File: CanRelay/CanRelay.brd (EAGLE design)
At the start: 93 x 65.5 mm, 21 parts

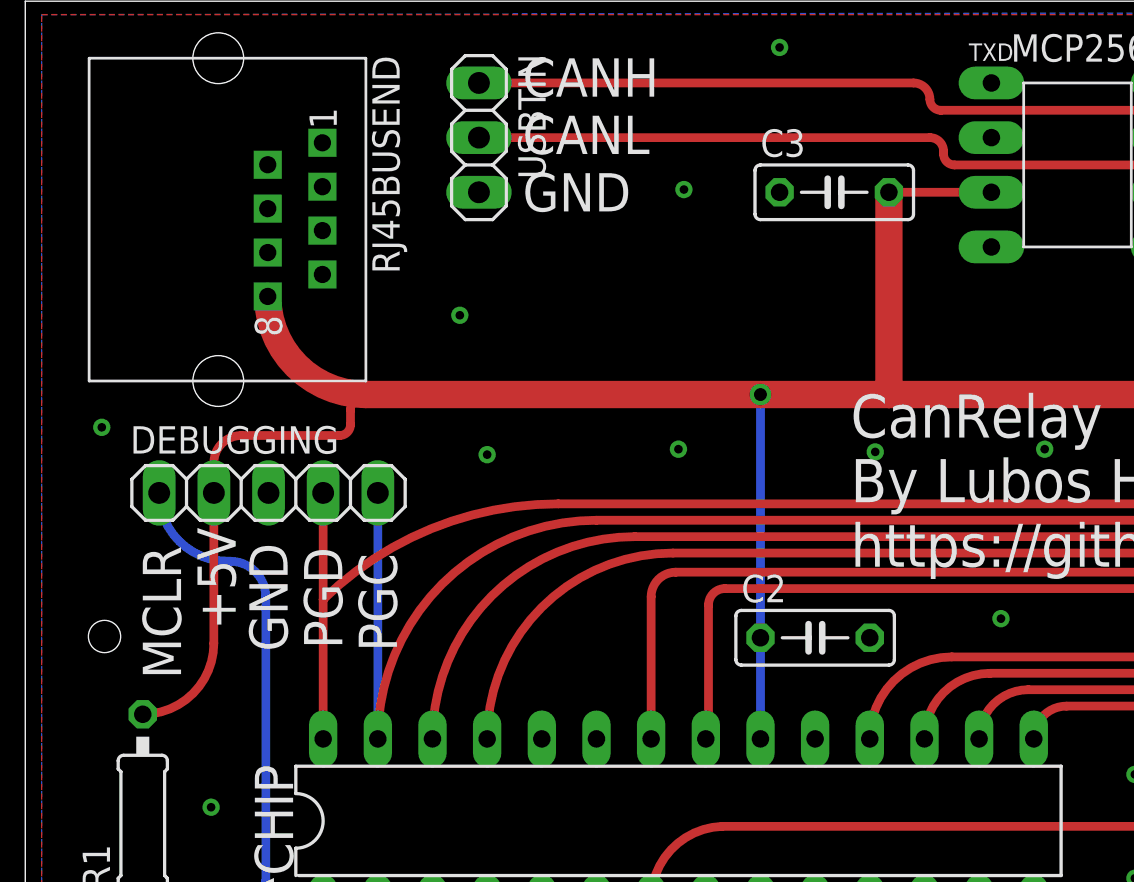
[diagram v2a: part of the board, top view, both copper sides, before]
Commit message: #10 mirroring pins on RJ45 and wiring up remainder to +5V and GND in schematic. Started work in board - rewired all +5V in thicker wire everywhere. wired up RJ45 +5V and GND pins, CAN lines and RX and TX lines between transceiver and chip unwire now still
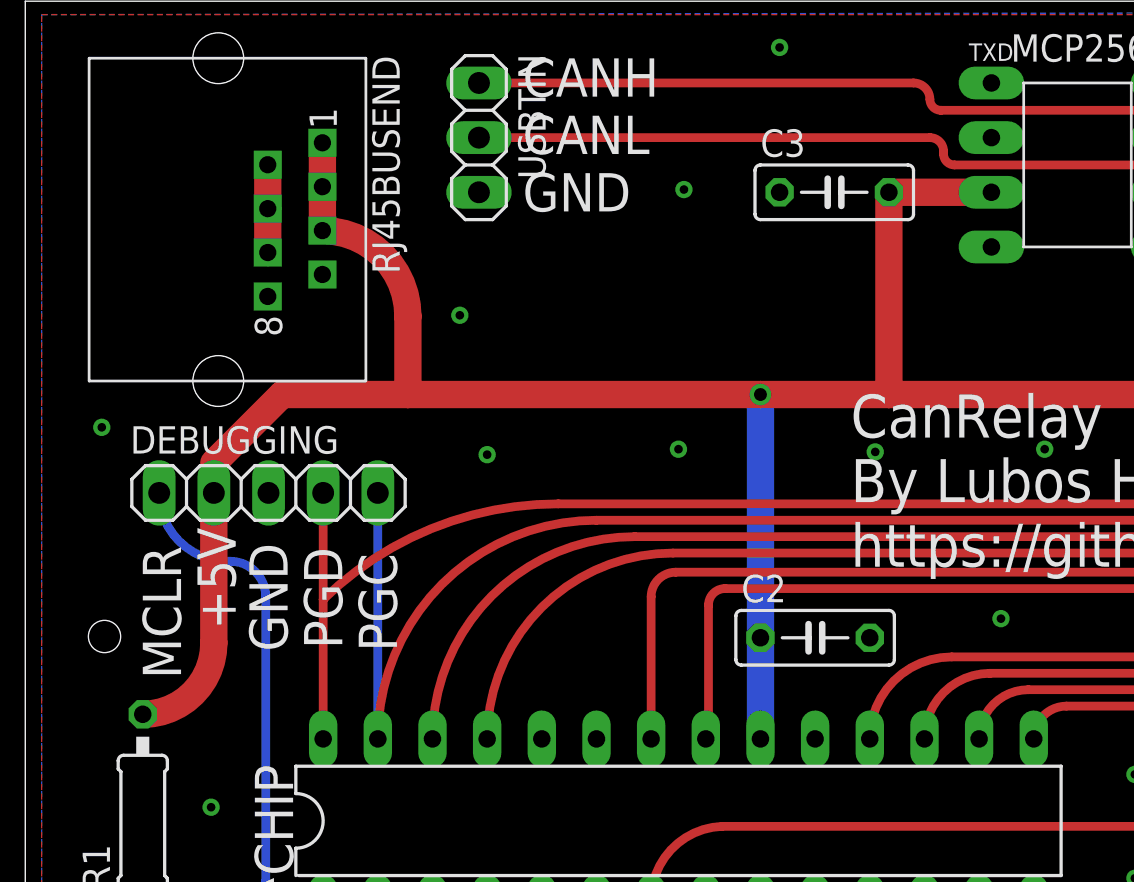
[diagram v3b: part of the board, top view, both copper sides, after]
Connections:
- net +5V: now also RJ45BUSEND.RJ45_1, RJ45BUSEND.RJ45_3, RJ45BUSEND.RJ45_5; no longer RJ45BUSEND.RJ45_8
- net CANH: now also RJ45BUSEND.RJ45_8; no longer RJ45BUSEND.RJ45_1
- net CANL: now also RJ45BUSEND.RJ45_7; no longer RJ45BUSEND.RJ45_2
- net GND: now also RJ45BUSEND.RJ45_2, RJ45BUSEND.RJ45_4, RJ45BUSEND.RJ45_6; no longer RJ45BUSEND.RJ45_3, RJ45BUSEND.RJ45_7
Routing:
- net +5V: track 134.8 -> 141.3 mm
- net GND: track 0.00 -> 4.08 mm
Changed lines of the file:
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@@
 <contactref element="C3" pad="2"/>
 <contactref element="DEBUGGING" pad="2"/>
-<contactref element="RJ45BUSEND" pad="RJ45_8"/>
 <contactref element="PWR" pad="VCC"/>
-<wire x1="40.132" y1="56.642" x2="44.895" y2="56.642" width="0.4064" layer="1"/>
 <wire x1="80.4" y1="47.244" x2="77.724" y2="47.244" width="1.27" layer="1"/>
 <wire x1="77.724" y1="47.244" x2="40.132" y2="47.244" width="1.27" layer="1"/>
 <wire x1="40.132" y1="47.244" x2="34.163" y2="47.244" width="1.27" layer="1"/>
 <wire x1="8.763" y1="41.783" x2="8.763" y2="42.672" width="0.4064" layer="1"/>
-<wire x1="5.461" y1="32.385" x2="8.763" y2="35.687" width="0.4064" layer="1" curve="90"/>
-<wire x1="8.763" y1="35.687" x2="8.763" y2="42.672" width="0.4064" layer="1"/>
 <via x="34.163" y="47.244" extent="1-16" drill="0.6" shape="square"/>
-<wire x1="34.163" y1="47.244" x2="34.163" y2="35.941" width="0.4064" layer="16"/>
-<wire x1="34.163" y1="35.941" x2="34.163" y2="31.242" width="0.4064" layer="16"/>
-<wire x1="34.163" y1="47.244" x2="15.826" y2="47.244" width="1.27" layer="1"/>
-<wire x1="11.268" y1="51.802" x2="15.826" y2="47.244" width="1.27" layer="1" curve="90"/>
-<wire x1="15.826" y1="47.244" x2="15.113" y2="46.531" width="0.4064" layer="1" curve="90"/>
-<wire x1="15.113" y1="46.531" x2="15.113" y2="45.847" width="0.4064" layer="1"/>
-<wire x1="15.113" y1="45.847" x2="14.605" y2="45.339" width="0.4064" layer="1" curve="-90"/>
-<wire x1="14.605" y1="45.339" x2="10.033" y2="45.339" width="0.4064" layer="1"/>
-<wire x1="10.033" y1="45.339" x2="8.763" y2="44.069" width="0.4064" layer="1" curve="90"/>
+<wire x1="34.163" y1="47.244" x2="17.78" y2="47.244" width="1.27" layer="1"/>
 <wire x1="8.763" y1="44.069" x2="8.763" y2="42.672" width="0.4064" layer="1"/>
 <contactref element="PWR1" pad="VCC"/>
@@
 <wire x1="40.132" y1="56.642" x2="40.132" y2="47.244" width="1.27" layer="1"/>
 <wire x1="77.724" y1="50.524" x2="83" y2="55.8" width="1.27" layer="1" curve="-90"/>
+<contactref element="RJ45BUSEND" pad="RJ45_1"/>
+<contactref element="RJ45BUSEND" pad="RJ45_3"/>
+<contactref element="RJ45BUSEND" pad="RJ45_5"/>
+<wire x1="13.808" y1="58.942" x2="13.808" y2="56.902" width="1.27" layer="1"/>
+<wire x1="13.808" y1="56.902" x2="13.808" y2="54.862" width="1.27" layer="1"/>
+<wire x1="13.808" y1="54.862" x2="17.78" y2="50.89" width="1.27" layer="1" curve="-90"/>
+<wire x1="17.78" y1="50.89" x2="17.78" y2="47.244" width="1.27" layer="1"/>
+<wire x1="8.763" y1="44.069" x2="11.938" y2="47.244" width="1.27" layer="1"/>
+<wire x1="11.938" y1="47.244" x2="17.78" y2="47.244" width="1.27" layer="1"/>
+<wire x1="44.895" y1="56.642" x2="40.132" y2="56.642" width="1.27" layer="1"/>
+<wire x1="5.461" y1="32.385" x2="8.763" y2="35.687" width="1.27" layer="1" curve="90"/>
+<wire x1="8.763" y1="35.687" x2="8.763" y2="42.672" width="1.27" layer="1"/>
+<wire x1="34.163" y1="47.244" x2="34.163" y2="35.941" width="1.27" layer="16"/>
+<wire x1="34.163" y1="35.941" x2="34.163" y2="31.242" width="1.27" layer="16"/>
 </signal>
 <signal name="GND">
@@
 <contactref element="DEBUGGING" pad="3"/>
 <contactref element="CSPLIT" pad="1"/>
-<contactref element="RJ45BUSEND" pad="RJ45_7"/>
-<contactref element="RJ45BUSEND" pad="RJ45_3"/>
 <contactref element="PWR" pad="GND1"/>
 <contactref element="PWR" pad="GND2"/>
@@
 <contactref element="PWR1" pad="GND2"/>
 <contactref element="PWR1" pad="GND1"/>
+<contactref element="RJ45BUSEND" pad="RJ45_2"/>
+<contactref element="RJ45BUSEND" pad="RJ45_4"/>
+<contactref element="RJ45BUSEND" pad="RJ45_6"/>
+<wire x1="11.268" y1="57.922" x2="11.268" y2="55.882" width="1.27" layer="1"/>
+<wire x1="11.268" y1="55.882" x2="11.268" y2="53.842" width="1.27" layer="1"/>
 </signal>
 <signal name="N$2">
@@
 <contactref element="MCP2561" pad="CANH"/>
 <contactref element="RSPLIT2" pad="2"/>
-<contactref element="RJ45BUSEND" pad="RJ45_1"/>
 <wire x1="56.896" y1="59.69" x2="56.388" y2="59.182" width="0.4064" layer="1" curve="-90"/>
 <wire x1="56.388" y1="59.182" x2="52.895" y2="59.182" width="0.4064" layer="1"/>
@@
 <wire x1="42.545" y1="60.452" x2="42.037" y2="60.96" width="0.4064" layer="1" curve="-90"/>
 <wire x1="42.037" y1="60.96" x2="41.275" y2="61.722" width="0.4064" layer="1" curve="90"/>
-<wire x1="13.808" y1="58.942" x2="21.082" y2="61.722" width="0" layer="19" extent="1-1"/>
+<contactref element="RJ45BUSEND" pad="RJ45_8"/>
+<wire x1="11.268" y1="51.802" x2="21.082" y2="61.722" width="0" layer="19" extent="1-1"/>
 </signal>
 <signal name="CANL">
 <contactref element="MCP2561" pad="CANL"/>
 <contactref element="RSPLIT1" pad="1"/>
-<contactref element="RJ45BUSEND" pad="RJ45_2"/>
 <wire x1="56.896" y1="56.007" x2="56.261" y2="56.642" width="0.4064" layer="1" curve="90"/>
 <wire x1="56.261" y1="56.642" x2="52.895" y2="56.642" width="0.4064" layer="1"/>
@@
 <wire x1="42.672" y1="58.547" x2="42.672" y2="58.42" width="0.4064" layer="1"/>
 <wire x1="42.672" y1="58.42" x2="43.18" y2="57.912" width="0.4064" layer="1" curve="90"/>
-<wire x1="11.268" y1="57.922" x2="21.082" y2="59.182" width="0" layer="19" extent="1-1"/>
+<contactref element="RJ45BUSEND" pad="RJ45_7"/>
+<wire x1="13.808" y1="52.822" x2="21.082" y2="59.182" width="0" layer="19" extent="1-1"/>
 </signal>
 <signal name="TXD">

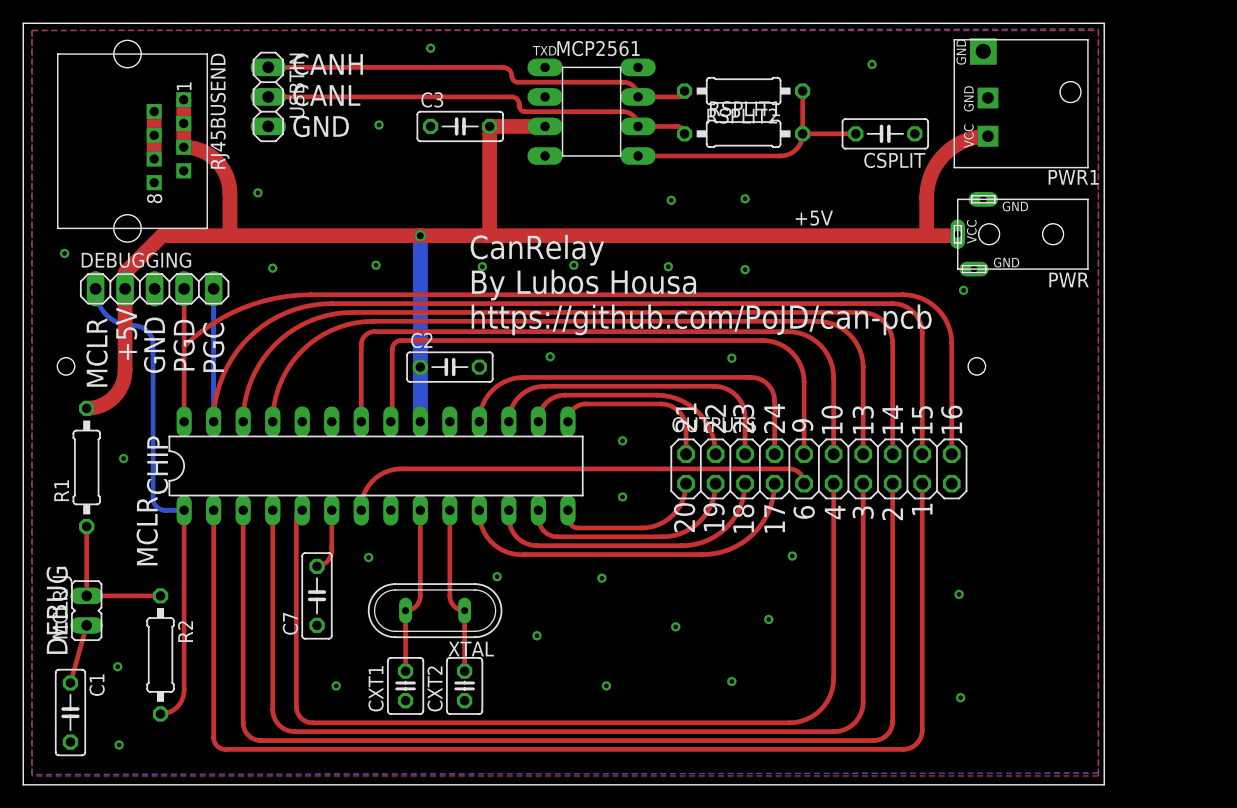
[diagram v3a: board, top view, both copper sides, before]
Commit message: #10 rerouting unwired connections, moving old power jack a bit lower to have more space for the actual jack plug. routed TXD and RXD too. Missing checking all at home with the actual plug sizes, adding more GND vias, running electrical checks
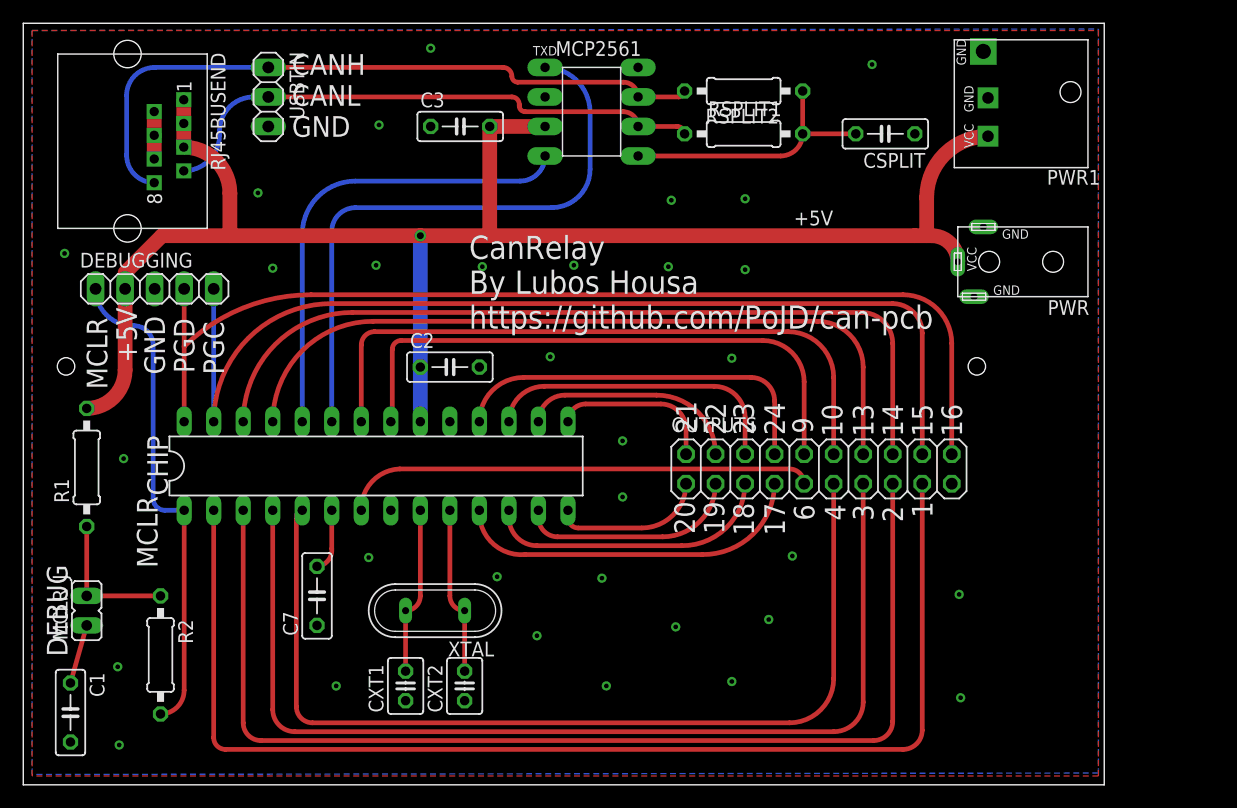
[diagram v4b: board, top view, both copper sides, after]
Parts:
- moved PWR 2.37 mm to (86.0, 45.0)
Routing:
- net TXD: track 0.18 -> 51.4 mm
- net RXD: track 0.00 -> 39.8 mm
- net CANH: track 37.1 -> 58.8 mm
- net CANL: track 37.2 -> 47.3 mm
- net +5V: track 141.3 -> 142.1 mm
- net GND: vias 33 -> 32
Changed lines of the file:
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@@
 <element name="MCP2561" library="PoJD" package="MCP2561_PDIP" value="MCP2561MCP" x="48.895" y="57.912"/>
 <element name="OUTPUTS" library="pinhead" package="2X10" value="" x="68.453" y="27.178"/>
-<element name="PWR" library="PoJD" package="DC-JACK-GK0.65" value="DC-JACK-GK0.65S" x="86" y="47.371" rot="R180"/>
+<element name="PWR" library="PoJD" package="DC-JACK-GK0.65" value="DC-JACK-GK0.65S" x="86" y="45" rot="R180"/>
 <element name="R1" library="rcl" package="0207/10" value="10000" x="5.461" y="27.305" rot="R90"/>
 <element name="R2" library="rcl" package="0207/10" value="470" x="11.811" y="11.176" rot="R270"/>
@@
 <contactref element="DEBUGGING" pad="2"/>
 <contactref element="PWR" pad="VCC"/>
-<wire x1="80.4" y1="47.244" x2="77.724" y2="47.244" width="1.27" layer="1"/>
-<wire x1="77.724" y1="47.244" x2="40.132" y2="47.244" width="1.27" layer="1"/>
+<wire x1="77.724" y1="47.244" x2="76.708" y2="47.244" width="1.27" layer="1"/>
+<wire x1="76.708" y1="47.244" x2="40.132" y2="47.244" width="1.27" layer="1"/>
 <wire x1="40.132" y1="47.244" x2="34.163" y2="47.244" width="1.27" layer="1"/>
 <wire x1="8.763" y1="41.783" x2="8.763" y2="42.672" width="0.4064" layer="1"/>
@@
 <wire x1="8.763" y1="44.069" x2="8.763" y2="42.672" width="0.4064" layer="1"/>
 <contactref element="PWR1" pad="VCC"/>
-<wire x1="80.4" y1="47.244" x2="80.4" y2="47.371" width="1.27" layer="1"/>
 <wire x1="77.724" y1="50.524" x2="77.724" y2="47.244" width="1.27" layer="1"/>
 <wire x1="40.132" y1="56.642" x2="40.132" y2="47.244" width="1.27" layer="1"/>
@@
 <wire x1="34.163" y1="47.244" x2="34.163" y2="35.941" width="1.27" layer="16"/>
 <wire x1="34.163" y1="35.941" x2="34.163" y2="31.242" width="1.27" layer="16"/>
+<wire x1="80.4" y1="45" x2="78.156" y2="47.244" width="1.27" layer="1" curve="90"/>
+<wire x1="78.156" y1="47.244" x2="77.724" y2="47.244" width="1.27" layer="1"/>
 </signal>
 <signal name="GND">
@@
 <via x="45.339" y="36.83" extent="1-16" drill="0.4" shape="square"/>
 <via x="60.96" y="36.703" extent="1-16" drill="0.4" shape="square"/>
-<via x="80.899" y="42.545" extent="1-16" drill="0.4" shape="square"/>
 <via x="62.103" y="50.419" extent="1-16" drill="0.4" shape="square"/>
 <via x="55.753" y="50.292" extent="1-16" drill="0.4" shape="square"/>
@@
 <wire x1="42.037" y1="60.96" x2="41.275" y2="61.722" width="0.4064" layer="1" curve="90"/>
 <contactref element="RJ45BUSEND" pad="RJ45_8"/>
-<wire x1="11.268" y1="51.802" x2="21.082" y2="61.722" width="0" layer="19" extent="1-1"/>
+<wire x1="11.268" y1="51.802" x2="8.89" y2="54.18" width="0.4064" layer="16" curve="-90"/>
+<wire x1="8.89" y1="54.18" x2="8.89" y2="59.309" width="0.4064" layer="16"/>
+<wire x1="8.89" y1="59.309" x2="11.303" y2="61.722" width="0.4064" layer="16" curve="-90"/>
+<wire x1="11.303" y1="61.722" x2="21.082" y2="61.722" width="0.4064" layer="16"/>
 </signal>
 <signal name="CANL">
@@
 <wire x1="42.672" y1="58.42" x2="43.18" y2="57.912" width="0.4064" layer="1" curve="90"/>
 <contactref element="RJ45BUSEND" pad="RJ45_7"/>
-<wire x1="13.808" y1="52.822" x2="21.082" y2="59.182" width="0" layer="19" extent="1-1"/>
+<wire x1="13.808" y1="52.822" x2="16.891" y2="55.905" width="0.4064" layer="16" curve="90"/>
+<wire x1="16.891" y1="55.905" x2="16.891" y2="56.261" width="0.4064" layer="16"/>
+<wire x1="16.891" y1="56.261" x2="19.812" y2="59.182" width="0.4064" layer="16" curve="-90"/>
+<wire x1="19.812" y1="59.182" x2="21.082" y2="59.182" width="0.4064" layer="16"/>
 </signal>
 <signal name="TXD">
@@
 <contactref element="CHIP" pad="23"/>
 <wire x1="26.543" y1="31.242" x2="26.67" y2="31.369" width="0.4064" layer="16" curve="90"/>
-<wire x1="26.67" y1="31.369" x2="44.895" y2="61.722" width="0" layer="19" extent="16-16"/>
+<wire x1="44.895" y1="61.722" x2="48.768" y2="57.849" width="0.4064" layer="16" curve="-90"/>
+<wire x1="48.768" y1="57.849" x2="48.768" y2="52.959" width="0.4064" layer="16"/>
+<wire x1="48.768" y1="52.959" x2="45.466" y2="49.657" width="0.4064" layer="16" curve="-90"/>
+<wire x1="45.466" y1="49.657" x2="28.575" y2="49.657" width="0.4064" layer="16"/>
+<wire x1="28.575" y1="49.657" x2="26.543" y2="47.625" width="0.4064" layer="16" curve="90"/>
+<wire x1="26.543" y1="47.625" x2="26.543" y2="31.242" width="0.4064" layer="16"/>
 </signal>
 <signal name="RXD">
 <contactref element="MCP2561" pad="RXD"/>
 <contactref element="CHIP" pad="24"/>
-<wire x1="24.003" y1="31.242" x2="44.895" y2="54.102" width="0" layer="19" extent="1-1"/>
+<wire x1="44.895" y1="54.102" x2="42.736" y2="51.943" width="0.4064" layer="16" curve="-90"/>
+<wire x1="42.736" y1="51.943" x2="28.575" y2="51.943" width="0.4064" layer="16"/>
+<wire x1="28.575" y1="51.943" x2="24.003" y2="47.371" width="0.4064" layer="16" curve="90"/>
+<wire x1="24.003" y1="47.371" x2="24.003" y2="31.242" width="0.4064" layer="16"/>
 </signal>
 <signal name="OSC2">
